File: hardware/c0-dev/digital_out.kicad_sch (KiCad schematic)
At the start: 11 parts, among them U33 B0505S-1WR3, U35 TCA9555PWR, U36 ISO1540

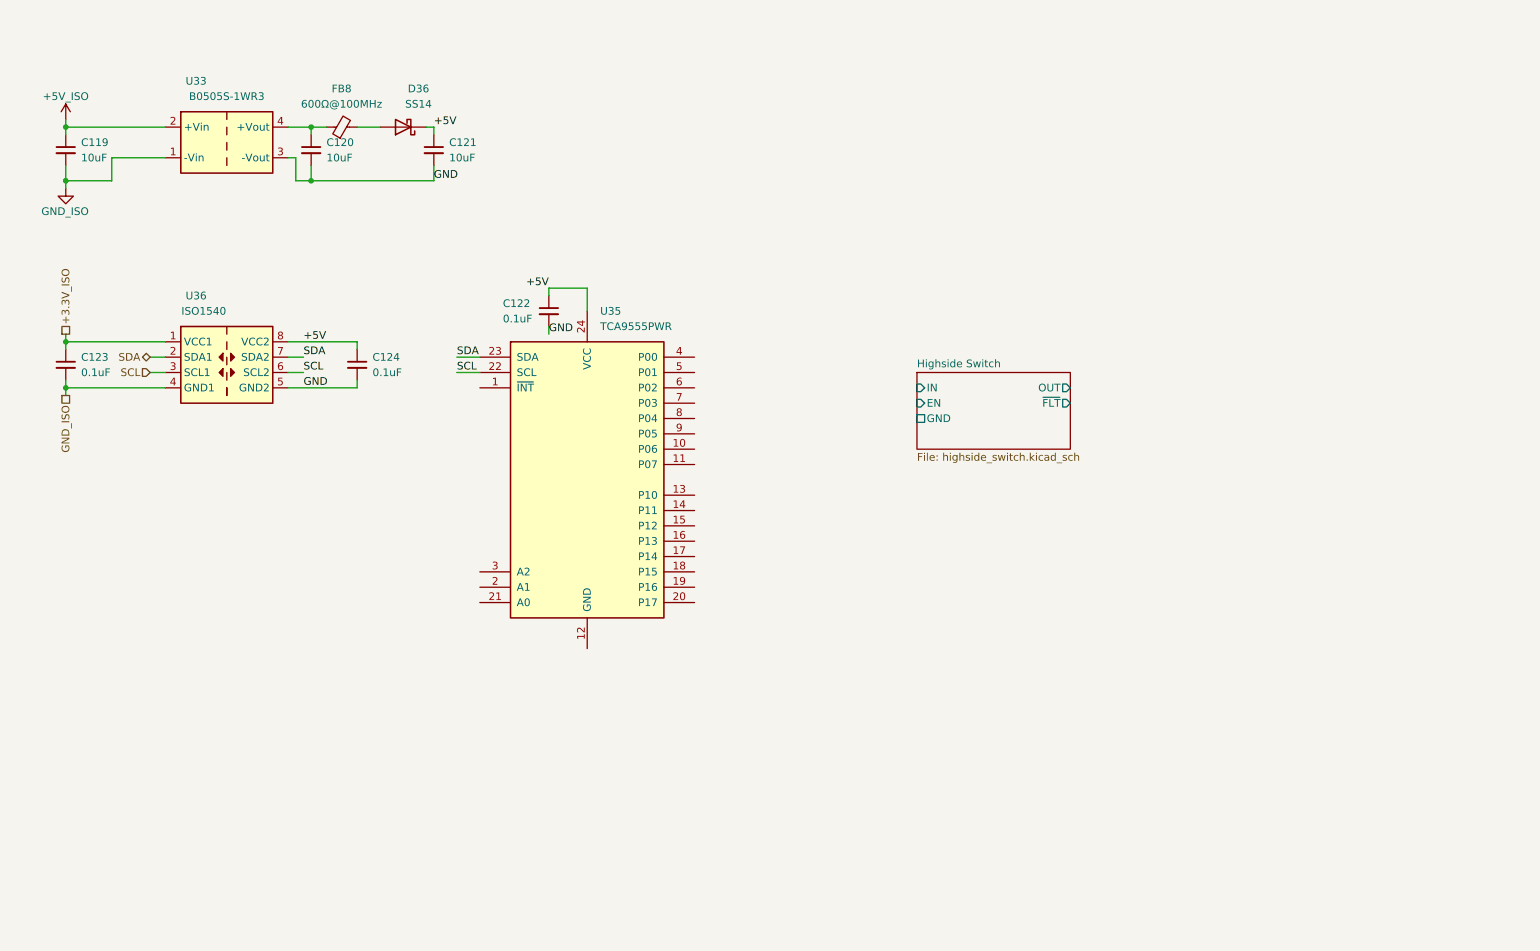
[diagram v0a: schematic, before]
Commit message: added DO
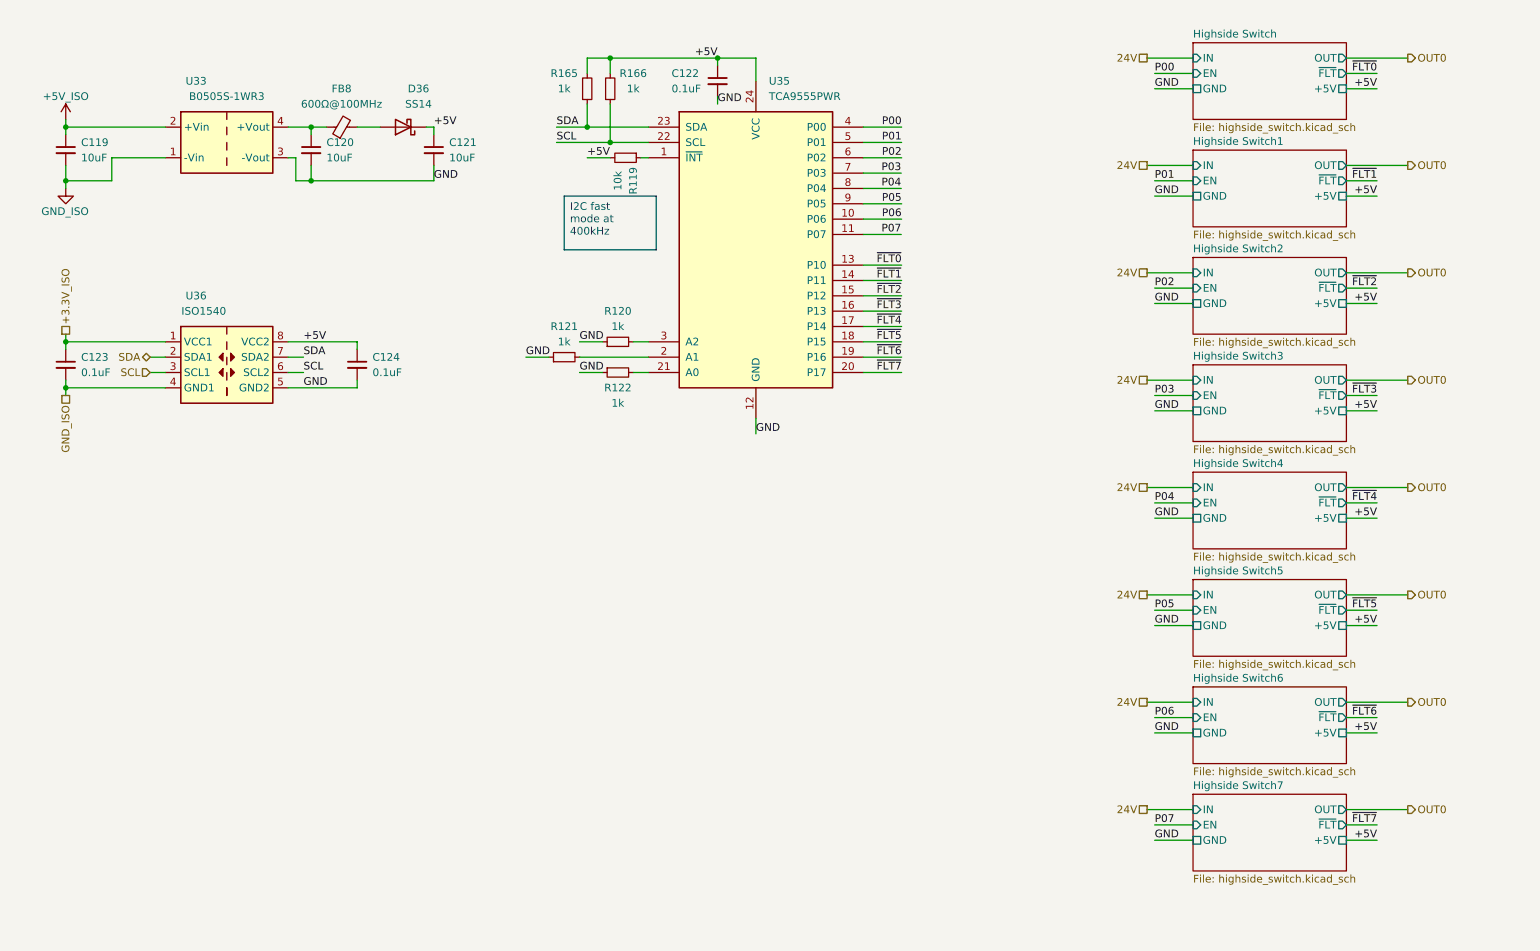
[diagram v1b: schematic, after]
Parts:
- added R119: 10k, Resistor_SMD:R_0402_1005Metric, symbol Device:R_Small
- added R120, R121, R122, R165, R166: 1k, Resistor_SMD:R_0402_1005Metric, symbol Device:R_Small
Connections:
- net +5V: now also R119.2, R165.2, R166.2
- net GND: now also U35.12 (GND), R120.1, R121.1, R122.1
- net SCL: now also R166.1
- net SDA: now also R165.1
- net at U35.1 (~{INT}): now also R119.1
- net P06: now reaches U35.10 (P06)
- net P07: now reaches U35.11 (P07)
- net ~{FLT0}: now reaches U35.13 (P10)
- net ~{FLT1}: now reaches U35.14 (P11)
- net ~{FLT2}: now reaches U35.15 (P12)
- net ~{FLT3}: now reaches U35.16 (P13)
- net ~{FLT4}: now reaches U35.17 (P14)
- net ~{FLT5}: now reaches U35.18 (P15)
- net ~{FLT6}: now reaches U35.19 (P16)
- net at U35.2 (A1): now also R121.2
- net ~{FLT7}: now reaches U35.20 (P17)
- net at U35.21 (A0): now also R122.2
- net at U35.3 (A2): now also R120.2
- net P00: now reaches U35.4 (P00)
- net P01: now reaches U35.5 (P01)
- net P02: now reaches U35.6 (P02)
- net P03: now reaches U35.7 (P03)
- net P04: now reaches U35.8 (P04)
- net P05: now reaches U35.9 (P05)
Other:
- added sheet Highside Switch1 (highside_switch.kicad_sch)
- added sheet Highside Switch2 (highside_switch.kicad_sch)
- added sheet Highside Switch3 (highside_switch.kicad_sch)
- added sheet Highside Switch4 (highside_switch.kicad_sch)
- added sheet Highside Switch5 (highside_switch.kicad_sch)
- added sheet Highside Switch6 (highside_switch.kicad_sch)
- added sheet Highside Switch7 (highside_switch.kicad_sch)
- sheet Highside Switch ports: added +5V; removed none
- moved on the sheet: C122, U35

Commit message: i2c address check
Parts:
- renumbered C119 to C116, C123 to C117, C120 to C118, C124 to C119, C121 to C120, C122 to C121, R121 to R114, R165 to R115, R166 to R116, R120 to R117, R122 to R118, U36 to U34
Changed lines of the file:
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@@
 	(generator_version "10.0")
 	(paper "A4")
+	(text_box "0x40"
+		(exclude_from_sim no)
+		(at 120.65 83.82 0)
+		(size 16.51 6.35)
+		(margins 0.9525 0.9525 0.9525 0.9525)
+		(stroke
+			(width 0)
+			(type solid)
+		)
+		(fill
+			(type none)
+		)
+		(effects
+			(font
+				(size 1.27 1.27)
+			)
+			(justify left top)
+		)
+	)
 	(text_box "I2C fast mode at 400kHz"
 		(exclude_from_sim no)
-		(at 119.38 46.99 0)
+		(at 119.38 48.26 0)
 		(size 15.24 8.89)
 		(margins 0.9525 0.9525 0.9525 0.9525)
@@
 		)
 	)
-	(hierarchical_label "OUT0"
+	(hierarchical_label "OUT7"
 		(shape output)
 		(at 259.08 148.59 0)
@@
 		)
 	)
-	(hierarchical_label "OUT0"
+	(hierarchical_label "OUT4"
 		(shape output)
 		(at 259.08 95.25 0)
@@
 		)
 	)
-	(hierarchical_label "OUT0"
+	(hierarchical_label "OUT3"
 		(shape output)
 		(at 259.08 77.47 0)
@@
 		)
 	)
-	(hierarchical_label "OUT0"
+	(hierarchical_label "OUT2"
 		(shape output)
 		(at 259.08 59.69 0)
@@
 		)
 	)
-	(hierarchical_label "OUT0"
+	(hierarchical_label "OUT5"
 		(shape output)
 		(at 259.08 113.03 0)
@@
 		)
 	)
-	(hierarchical_label "OUT0"
+	(hierarchical_label "OUT1"
 		(shape output)
 		(at 259.08 41.91 0)
@@
 		)
 	)
-	(hierarchical_label "OUT0"
+	(hierarchical_label "OUT6"
 		(shape output)
 		(at 259.08 130.81 0)
@@
 		(in_pos_files yes)
 		(dnp no)
-		(property "Reference" "R120"
+		(property "Reference" "R117"
 			(at 128.27 66.04 90)
 			(show_name no)
@@
 			(project "c0-dev"
 				(path "/b8347a0e-ad04-4414-969d-3c64a611d74e/680032e3-5da4-48ad-9c49-e468cbbeffb9"
-					(reference "R120")
+					(reference "R117")
 					(unit 1)
 				)
@@
 		(in_pos_files yes)
 		(dnp no)
-		(property "Reference" "U36"
+		(property "Reference" "U34"
 			(at 58.42 63.5 0)
 			(show_name no)
@@
 			(project "c0-dev"
 				(path "/b8347a0e-ad04-4414-969d-3c64a611d74e/680032e3-5da4-48ad-9c49-e468cbbeffb9"
-					(reference "U36")
+					(reference "U34")
 					(unit 1)
 				)
@@
 		(dnp no)
 		(fields_autoplaced yes)
-		(property "Reference" "C119"
+		(property "Reference" "C116"
 			(at 39.37 38.1062 0)
 			(show_name no)
@@
 			(project "c0-dev"
 				(path "/b8347a0e-ad04-4414-969d-3c64a611d74e/680032e3-5da4-48ad-9c49-e468cbbeffb9"
-					(reference "C119")
+					(reference "C116")
 					(unit 1)
 				)
@@
 		(in_pos_files yes)
 		(dnp no)
-		(property "Reference" "R166"
+		(property "Reference" "R116"
 			(at 130.81 26.67 0)
 			(show_name no)
@@
 			(project "c0-dev"
 				(path "/b8347a0e-ad04-4414-969d-3c64a611d74e/680032e3-5da4-48ad-9c49-e468cbbeffb9"
-					(reference "R166")
+					(reference "R116")
 					(unit 1)
 				)
@@
 		(in_pos_files yes)
 		(dnp no)
-		(property "Reference" "#PWR084"
+		(property "Reference" "#PWR086"
 			(at 36.83 52.07 0)
 			(hide yes)
@@
 			(project "c0-dev"
 				(path "/b8347a0e-ad04-4414-969d-3c64a611d74e/680032e3-5da4-48ad-9c49-e468cbbeffb9"
-					(reference "#PWR084")
+					(reference "#PWR086")
 					(unit 1)
 				)
@@
 		(in_pos_files yes)
 		(dnp no)
-		(property "Reference" "R122"
+		(property "Reference" "R118"
 			(at 128.27 78.74 90)
 			(show_name no)
@@
 			(project "c0-dev"
 				(path "/b8347a0e-ad04-4414-969d-3c64a611d74e/680032e3-5da4-48ad-9c49-e468cbbeffb9"
-					(reference "R122")
+					(reference "R118")
 					(unit 1)
 				)
@@
 		(dnp no)
 		(fields_autoplaced yes)
-		(property "Reference" "C121"
+		(property "Reference" "C120"
 			(at 100.33 38.1062 0)
 			(show_name no)
@@
 			(project "c0-dev"
 				(path "/b8347a0e-ad04-4414-969d-3c64a611d74e/680032e3-5da4-48ad-9c49-e468cbbeffb9"
-					(reference "C121")
+					(reference "C120")
 					(unit 1)
 				)
@@
 		(dnp no)
 		(fields_autoplaced yes)
-		(property "Reference" "C123"
+		(property "Reference" "C117"
 			(at 39.37 73.6662 0)
 			(show_name no)
@@
 			(project "c0-dev"
 				(path "/b8347a0e-ad04-4414-969d-3c64a611d74e/680032e3-5da4-48ad-9c49-e468cbbeffb9"
-					(reference "C123")
+					(reference "C117")
 					(unit 1)
 				)
@@
 		(dnp no)
 		(fields_autoplaced yes)
-		(property "Reference" "C124"
+		(property "Reference" "C119"
 			(at 87.63 73.6662 0)
 			(show_name no)
@@
 			(project "c0-dev"
 				(path "/b8347a0e-ad04-4414-969d-3c64a611d74e/680032e3-5da4-48ad-9c49-e468cbbeffb9"
-					(reference "C124")
+					(reference "C119")
 					(unit 1)
 				)
@@
 		(in_pos_files yes)
 		(dnp no)
-		(property "Reference" "R121"
+		(property "Reference" "R114"
 			(at 119.38 68.58 90)
 			(show_name no)
@@
 			(project "c0-dev"
 				(path "/b8347a0e-ad04-4414-969d-3c64a611d74e/680032e3-5da4-48ad-9c49-e468cbbeffb9"
-					(reference "R121")
+					(reference "R114")
 					(unit 1)
 				)
@@
 		(dnp no)
 		(fields_autoplaced yes)
-		(property "Reference" "C120"
+		(property "Reference" "C118"
 			(at 80.01 38.1062 0)
 			(show_name no)
@@
 			(project "c0-dev"
 				(path "/b8347a0e-ad04-4414-969d-3c64a611d74e/680032e3-5da4-48ad-9c49-e468cbbeffb9"
-					(reference "C120")
+					(reference "C118")
 					(unit 1)
 				)
@@
 		(in_pos_files yes)
 		(dnp no)
-		(property "Reference" "R165"
+		(property "Reference" "R115"
 			(at 119.38 26.67 0)
 			(show_name no)
@@
 			(project "c0-dev"
 				(path "/b8347a0e-ad04-4414-969d-3c64a611d74e/680032e3-5da4-48ad-9c49-e468cbbeffb9"
-					(reference "R165")
+					(reference "R115")
 					(unit 1)
 				)
@@
 		(in_pos_files yes)
 		(dnp no)
-		(property "Reference" "#PWR083"
+		(property "Reference" "#PWR085"
 			(at 36.83 38.1 0)
 			(hide yes)
@@
 			(project "c0-dev"
 				(path "/b8347a0e-ad04-4414-969d-3c64a611d74e/680032e3-5da4-48ad-9c49-e468cbbeffb9"
-					(reference "#PWR083")
+					(reference "#PWR085")
 					(unit 1)
 				)
@@
 		(in_pos_files yes)
 		(dnp no)
-		(property "Reference" "C122"
+		(property "Reference" "C121"
 			(at 137.16 26.67 0)
 			(show_name no)
@@
 			(project "c0-dev"
 				(path "/b8347a0e-ad04-4414-969d-3c64a611d74e/680032e3-5da4-48ad-9c49-e468cbbeffb9"
-					(reference "C122")
+					(reference "C121")
 					(unit 1)
 				)

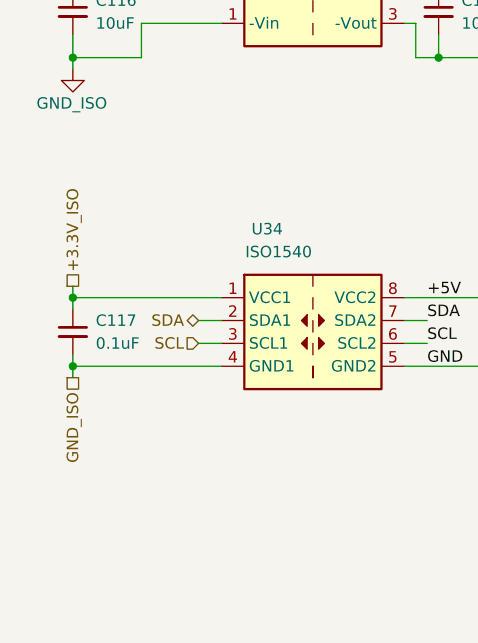
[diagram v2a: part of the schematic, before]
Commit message: introduced MCU isolation netclass
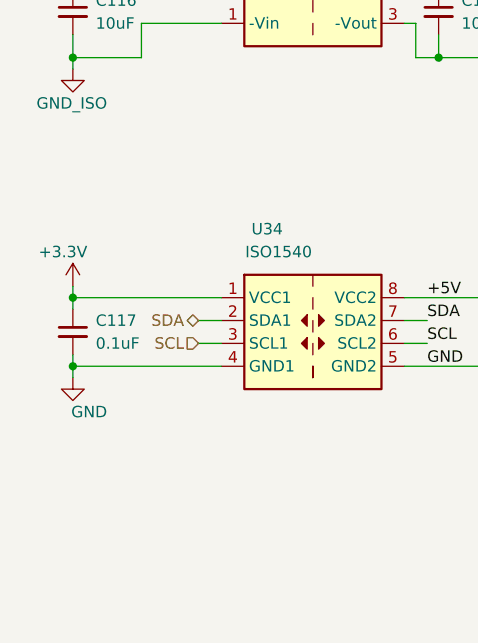
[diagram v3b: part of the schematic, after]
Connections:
- net GND: now also C117.2, U34.4 (GND1)
- net GND_ISO: no longer C117.2, U34.4 (GND1)
- net +3.3V_ISO renamed +3.3V
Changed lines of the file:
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@@
-		)
-	)
-	(hierarchical_label "GND_ISO"
-		(shape passive)
-		(at 36.83 80.01 270)
-		(effects
-			(font
-				(size 1.27 1.27)
-			)
-			(justify right)
 		)
 	)
@@
 		)
 	)
-	(hierarchical_label "+3.3V_ISO"
-		(shape passive)
-		(at 36.83 69.85 90)
-		(effects
-			(font
-				(size 1.27 1.27)
-			)
-			(justify left)
-		)
-	)
 	(hierarchical_label "24V"
 		(shape passive)
@@
 		(polyline
 			(pts
-				(xy 25.4 25.4) (xy 63.5 25.4) (xy 63.5 107.95) (xy 25.4 107.95)
+				(xy 25.4 25.4) (xy 63.5 25.4) (xy 63.5 53.34) (xy 25.4 53.34)
+			)
+			(stroke
+				(width 0)
+				(type dash)
+			)
+			(fill
+				(type none)
+			)
+		)
+	)
+	(rule_area
+		(exclude_from_sim no)
+		(in_bom yes)
+		(on_board yes)
+		(dnp no)
+		(polyline
+			(pts
+				(xy 25.4 59.69) (xy 63.5 59.69) (xy 63.5 87.63) (xy 25.4 87.63)
 			)
 			(stroke
@@
 		)
 	)
+	(netclass_flag ""
+		(length 2.54)
+		(shape round)
+		(at 25.4 59.69 0)
+		(fields_autoplaced yes)
+		(effects
+			(font
+				(size 1.27 1.27)
+			)
+			(justify left bottom)
+		)
+		(property "Net Class" "Isolated_MCU"
+			(at 26.0985 57.15 0)
+			(show_name no)
+			(do_not_autoplace no)
+			(effects
+				(font
+					(size 1.27 1.27)
+				)
+				(justify left)
+			)
+		)
+		(property "Component Class" ""
+			(at -151.13 26.67 0)
+			(show_name no)
+			(do_not_autoplace no)
+			(effects
+				(font
+					(size 1.27 1.27)
+					(italic yes)
+				)
+			)
+		)
+	)
 	(symbol
 		(lib_id "Device:R_Small")
@@
 				(path "/b8347a0e-ad04-4414-969d-3c64a611d74e/680032e3-5da4-48ad-9c49-e468cbbeffb9"
 					(reference "R119")
+					(unit 1)
+				)
+			)
+		)
+	)
+	(symbol
+		(lib_id "power:+12V")
+		(at 36.83 69.85 0)
+		(unit 1)
+		(body_style 1)
+		(exclude_from_sim no)
+		(in_bom yes)
+		(on_board yes)
+		(in_pos_files yes)
+		(dnp no)
+		(property "Reference" "#PWR090"
+			(at 36.83 73.66 0)
+			(hide yes)
+			(show_name no)
+			(do_not_autoplace no)
+			(effects
+				(font
+					(size 1.27 1.27)
+				)
+			)
+		)
+		(property "Value" "+3.3V"
+			(at 33.02 66.04 0)
+			(show_name no)
+			(do_not_autoplace no)
+			(effects
+				(font
+					(size 1.27 1.27)
+				)
+				(justify left)
+			)
+		)
+		(property "Footprint" ""
+			(at 36.83 69.85 0)
+			(hide yes)
+			(show_name no)
+			(do_not_autoplace no)
+			(effects
+				(font
+					(size 1.27 1.27)
+				)
+			)
+		)
+		(property "Datasheet" ""
+			(at 36.83 69.85 0)
+			(hide yes)
+			(show_name no)
+			(do_not_autoplace no)
+			(effects
+				(font
+					(size 1.27 1.27)
+				)
+			)
+		)
+		(property "Description" "Power symbol creates a global label with name \"+12V\""
+			(at 36.83 69.85 0)
+			(hide yes)
+			(show_name no)
+			(do_not_autoplace no)
+			(effects
+				(font
+					(size 1.27 1.27)
+				)
+			)
+		)
+		(pin "1"
+		)
+		(instances
+			(project "c0-dev"
+				(path "/b8347a0e-ad04-4414-969d-3c64a611d74e/680032e3-5da4-48ad-9c49-e468cbbeffb9"
+					(reference "#PWR090")
 					(unit 1)
 				)
@@
 					(unit 1)
 				)
+			)
+		)
+	)
+	(symbol
+		(lib_id "power:GND")
+		(at 36.83 80.01 0)
+		(unit 1)
+		(body_style 1)
+		(exclude_from_sim no)
+		(in_bom yes)
+		(on_board yes)
+		(in_pos_files yes)
+		(dnp no)
+		(property "Reference" "#PWR091"
+			(at 36.83 86.36 0)
+			(hide yes)
+			(show_name no)
+			(do_not_autoplace no)
+			(effects
+				(font
+					(size 1.27 1.27)
+				)
+			)
+		)
+		(property "Value" "GND"
+			(at 40.64 83.82 0)
+			(show_name no)
+			(do_not_autoplace no)
+			(effects
+				(font
+					(size 1.27 1.27)
+				)
+				(justify right)
+			)
+		)
+		(property "Footprint" ""
+			(at 36.83 80.01 0)
+			(hide yes)
+			(show_name no)
+			(do_not_autoplace no)
+			(effects
+				(font
+					(size 1.27 1.27)
+				)
+			)
+		)
+		(property "Datasheet" ""
+			(at 36.83 80.01 0)
+			(hide yes)
+			(show_name no)
+			(do_not_autoplace no)
+			(effects
+				(font
+					(size 1.27 1.27)
+				)
+			)
+		)
+		(property "Description" "Power symbol creates a global label with name \"GND\" , ground"
+			(at 36.83 80.01 0)
+			(hide yes)
+			(show_name no)
+			(do_not_autoplace no)
+			(effects
+				(font
+					(size 1.27 1.27)
+				)
+			)
+		)
+		(pin "1"
+		)
+		(instances
+			(project "c0-dev"
+				(path "/b8347a0e-ad04-4414-969d-3c64a611d74e/680032e3-5da4-48ad-9c49-e468cbbeffb9"
+					(reference "#PWR091")
+					(unit 1)
+				)
